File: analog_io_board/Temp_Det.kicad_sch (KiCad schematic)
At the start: 3 parts, among them J3 DG141R-02, U8 MAX31855KASA (SOIC-8)

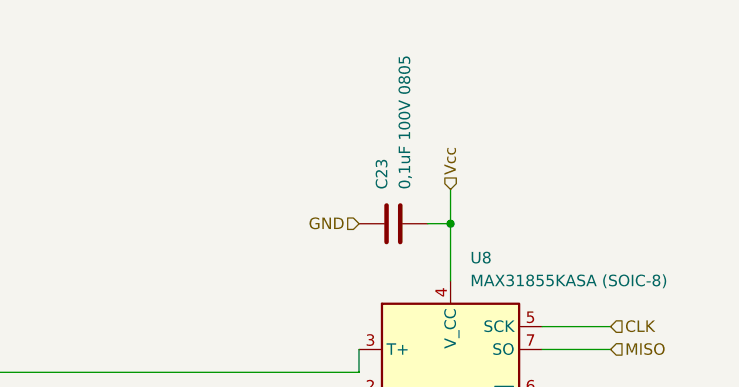
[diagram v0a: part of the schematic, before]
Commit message: all замменил резисторы failsafe в плате контроллера и обрал из перечня во всех остальных
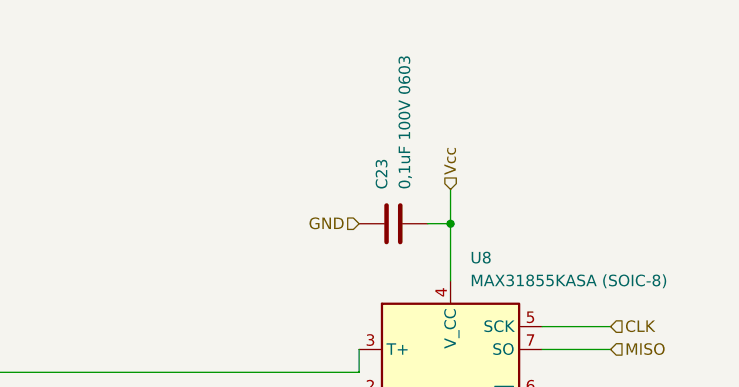
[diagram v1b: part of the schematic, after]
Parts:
- C23: value 0,1uF 100V 0805 -> 0,1uF 100V 0603; footprint Capacitor_SMD:C_0805_2012Metric_Pad1.18x1.45mm_HandSolder -> Capacitor_SMD:C_0603_1608Metric_Pad1.08x0.95mm_HandSolder

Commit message: analog board refresh
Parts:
- removed C23: 0,1uF 100V 0603, Capacitor_SMD:C_0603_1608Metric_Pad1.08x0.95mm_HandSolder, symbol Device:C
- removed J3: DG141R-02, Connector:DG141R-02, symbol Connector_Generic:Conn_01x02
- removed U8: MAX31855KASA (SOIC-8), Package_SO:SOIC-8_3.9x4.9mm_P1.27mm, symbol Sensor_Temperature:MAX31855KASA
- added C26, C27: 0,1uF 100V 0603, Capacitor_SMD:C_0603_1608Metric_Pad1.08x0.95mm_HandSolder, symbol Device:C
- added J5, J6: DG141R-2.54-03P-14-00A(H), symbol Connector:Conn_01x03_Socket
- added R18, R19, R20, R21: 0805-4,7 кОм±5%-0,125 Вт, PCM_4ms_Resistor:R_0805_2012Metric, symbol Device:R
- added TP21, TP22: TestPoint, PCM_4ms_TestPoint:TestPoint_D1, symbol Connector:TestPoint
- added U6, U8: DS18S20, Package_TO_SOT_THT:TO-92_Inline, symbol Sensor_Temperature:DS18S20
- added U7: π142M3x, Package_SO:SOIC-16_3.9x9.9mm_P1.27mm, symbol Isolator:π142M3x
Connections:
- new net: J6.2 (Pin_2), R19.1, TP22.1, U7.4 (VIB), U7.6 (VOD)
- new net: J5.2 (Pin_2), R18.1, TP21.1, U7.3 (VIA), U7.5 (VOC)
- new net: R20.2, U7.10 (VE2)
- new net: R21.1, U7.7 (VE1)
- new net +3.3VA: C27.2, J5.3 (Pin_3), J6.3 (Pin_3), R18.2, R19.2, R21.2, U7.1 (VDD1)
- new net +3V3: C26.2, R20.1, U7.16 (VDD2)
- new net GNDA: C27.1, J5.1 (Pin_1), J6.1 (Pin_1), U7.2 (GND1), U7.8 (GND1)
- new net GNDD: C26.1, U7.15 (GND2), U7.9 (GND2)
- new net RX_USART_2: U7.14 (VOA)
- new net RX_USART_4: U7.13 (VOB)
- new net TX_USART_2: U7.12 (VIC)
- new net TX_USART_4: U7.11 (VID)

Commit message: analog board refresh pcb
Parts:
- C26, C27: footprint Capacitor_SMD:C_0603_1608Metric_Pad1.08x0.95mm_HandSolder -> Capacitor_SMD:C_0603_1608Metric
- J6: footprint (none) -> Connector:DG141R-2.54-03P
- J7: renamed from J5; footprint (none) -> Connector:DG141R-2.54-03P
- R18, R19, R20, R21: footprint PCM_4ms_Resistor:R_0805_2012Metric -> Resistor_SMD:R_0805_2012Metric
- TP21, TP22: footprint PCM_4ms_TestPoint:TestPoint_D1 -> TestPoint:TestPoint_Pad_D1.0mm
- U7: value π142M3x -> PAI142M3x
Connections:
- no-connect marks 0 -> 6
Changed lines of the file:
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@@
 		(color 0 0 0 0)
+	)
+	(no_connect
+		(at 260.35 101.6)
+	)
+	(no_connect
+		(at 267.97 93.98)
+	)
+	(no_connect
+		(at 267.97 109.22)
+	)
+	(no_connect
+		(at 260.35 76.2)
+	)
+	(no_connect
+		(at 267.97 68.58)
+	)
+	(no_connect
+		(at 267.97 83.82)
 	)
 	(wire
@@
 			)
 		)
-		(property "Footprint" "PCM_4ms_TestPoint:TestPoint_D1"
+		(property "Footprint" "TestPoint:TestPoint_Pad_D1.0mm"
 			(at 137.16 83.82 0)
 			(effects
@@
 			)
 		)
-		(property "Description" ""
+		(property "Description" "test point"
 			(at 142.24 83.82 0)
 			(effects
@@
 			)
 		)
-		(property "Footprint" "PCM_4ms_Resistor:R_0805_2012Metric"
+		(property "Footprint" "Resistor_SMD:R_0805_2012Metric"
 			(at 166.878 99.06 90)
 			(effects
@@
 			)
 		)
-		(property "Description" ""
+		(property "Description" "Resistor"
 			(at 165.1 99.06 0)
 			(effects
@@
 			)
 		)
-		(property "Footprint" "PCM_4ms_Resistor:R_0805_2012Metric"
+		(property "Footprint" "Resistor_SMD:R_0805_2012Metric"
 			(at 163.322 73.66 90)
 			(effects
@@
 			)
 		)
-		(property "Description" ""
+		(property "Description" "Resistor"
 			(at 165.1 73.66 0)
 			(effects
@@
 			)
 		)
-		(property "Description" ""
+		(property "Description" "Power symbol creates a global label with name \"+3.3VA\""
 			(at 236.22 100.33 0)
 			(effects
@@
 	)
 	(symbol
-		(lib_id "PCM_4ms_Power-symbol:GNDA")
+		(lib_id "power:GNDA")
 		(at 114.3 73.66 0)
 		(mirror x)
@@
 			)
 		)
-		(property "Description" ""
+		(property "Description" "Power symbol creates a global label with name \"GNDA\" , analog ground"
 			(at 114.3 73.66 0)
 			(effects
@@
 			)
 		)
-		(property "Description" ""
+		(property "Description" "Power symbol creates a global label with name \"+3.3VA\""
 			(at 236.22 74.93 0)
 			(effects
@@
 		)
 		(property "Value" "GNDD"
-			(at 80.01 69.85 0)
+			(at 80.01 68.58 0)
 			(effects
 				(font
@@
 			)
 		)
-		(property "Description" ""
+		(property "Description" "Power symbol creates a global label with name \"GNDD\" , digital ground"
 			(at 80.01 73.66 0)
 			(effects
@@
 	)
 	(symbol
-		(lib_id "PCM_4ms_Power-symbol:GNDA")
+		(lib_id "power:GNDA")
 		(at 113.03 109.22 0)
 		(mirror y)
@@
 			)
 		)
-		(property "Description" ""
+		(property "Description" "Power symbol creates a global label with name \"GNDA\" , analog ground"
 			(at 113.03 109.22 0)
 			(effects
@@
 			)
 		)
-		(property "Description" ""
+		(property "Description" "Power symbol creates a global label with name \"GNDD\" , digital ground"
 			(at 45.72 132.08 0)
 			(effects
@@
 			)
 		)
-		(property "Value" "π142M3x"
+		(property "Value" "PAI142M3x"
 			(at 97.79 78.74 0)
 			(effects
@@
 			)
 		)
-		(property "Description" ""
+		(property "Description" "Power symbol creates a global label with name \"+3V3\""
 			(at 73.66 83.82 0)
 			(effects
@@
 			)
 		)
-		(property "Footprint" "Capacitor_SMD:C_0603_1608Metric_Pad1.08x0.95mm_HandSolder"
+		(property "Footprint" "Capacitor_SMD:C_0603_1608Metric"
 			(at 79.0448 81.28 0)
 			(effects
@@
 			)
 		)
-		(property "Description" ""
+		(property "Description" "Unpolarized capacitor"
 			(at 80.01 77.47 0)
 			(effects
@@
 			)
 		)
-		(property "Description" ""
+		(property "Description" "Power symbol creates a global label with name \"+3.3VA\""
 			(at 48.26 143.51 0)
 			(effects
@@
 			)
 		)
-		(property "Footprint" "PCM_4ms_Resistor:R_0805_2012Metric"
+		(property "Footprint" "Resistor_SMD:R_0805_2012Metric"
 			(at 118.11 99.822 90)
 			(effects
@@
 			)
 		)
-		(property "Description" ""
+		(property "Description" "Resistor"
 			(at 118.11 101.6 0)
 			(effects
@@
 		(dnp no)
 		(fields_autoplaced yes)
-		(property "Reference" "J5"
+		(property "Reference" "J7"
 			(at 240.665 69.85 0)
 			(effects
@@
 			)
 		)
-		(property "Footprint" ""
+		(property "Footprint" "Connector:DG141R-2.54-03P"
 			(at 241.3 77.47 0)
 			(effects
@@
 			(project "analog_io_board"
 				(path "/c658a069-2acb-41ac-8530-c56b14d342d1/c4e2dc63-ff36-4a03-a5b1-351b3374beb1"
-					(reference "J5")
+					(reference "J7")
 					(unit 1)
 				)
@@
 			)
 		)
-		(property "Description" ""
+		(property "Description" "Power symbol creates a global label with name \"GNDD\" , digital ground"
 			(at 82.55 107.95 0)
 			(effects
@@
 			)
 		)
-		(property "Description" ""
+		(property "Description" "Power symbol creates a global label with name \"+3V3\""
 			(at 45.72 124.46 0)
 			(effects
@@
 			)
 		)
-		(property "Description" ""
+		(property "Description" "Power symbol creates a global label with name \"+3.3VA\""
 			(at 115.57 83.82 0)
 			(effects
@@
 			)
 		)
-		(property "Footprint" ""
+		(property "Footprint" "Connector:DG141R-2.54-03P"
 			(at 241.3 102.87 0)
 			(effects
@@
 	)
 	(symbol
-		(lib_id "PCM_4ms_Power-symbol:GNDA")
+		(lib_id "power:GNDA")
 		(at 45.72 152.4 0)
 		(mirror y)
@@
 			)
 		)
-		(property "Description" ""
+		(property "Description" "Power symbol creates a global label with name \"GNDA\" , analog ground"
 			(at 45.72 152.4 0)
 			(effects
@@
 			)
 		)
-		(property "Description" ""
+		(property "Description" "Power symbol creates a global label with name \"+3V3\""
 			(at 72.39 101.6 0)
 			(effects
@@
 			)
 		)
-		(property "Footprint" "PCM_4ms_TestPoint:TestPoint_D1"
+		(property "Footprint" "TestPoint:TestPoint_Pad_D1.0mm"
 			(at 125.73 83.82 0)
 			(effects
@@
 			)
 		)
-		(property "Description" ""
+		(property "Description" "test point"
 			(at 130.81 83.82 0)
 			(effects
@@
 	)
 	(symbol
-		(lib_id "PCM_4ms_Power-symbol:GNDA")
+		(lib_id "power:GNDA")
 		(at 236.22 105.41 270)
 		(unit 1)
@@
 		)
 		(property "Value" "GNDA"
-			(at 232.41 105.4101 90)
+			(at 232.41 105.4099 90)
 			(effects
 				(font
@@
 			)
 		)
-		(property "Description" ""
+		(property "Description" "Power symbol creates a global label with name \"GNDA\" , analog ground"
 			(at 236.22 105.41 0)
 			(effects
@@
 			)
 		)
-		(property "Description" ""
+		(property "Description" "Power symbol creates a global label with name \"+3.3VA\""
 			(at 123.19 101.6 0)
 			(effects
@@
 	)
 	(symbol
-		(lib_id "PCM_4ms_Power-symbol:GNDA")
+		(lib_id "power:GNDA")
 		(at 236.22 80.01 270)
 		(unit 1)
@@
 		)
 		(property "Value" "GNDA"
-			(at 232.41 80.0101 90)
+			(at 232.41 80.0099 90)
 			(effects
 				(font
@@
 			)
 		)
-		(property "Description" ""
+		(property "Description" "Power symbol creates a global label with name \"GNDA\" , analog ground"
 			(at 236.22 80.01 0)
 			(effects
@@
 			)
 		)
-		(property "Description" ""
+		(property "Description" "Power symbol creates a global label with name \"+3.3VA\""
 			(at 165.1 104.14 0)
 			(effects
@@
 			)
 		)
-		(property "Footprint" "Capacitor_SMD:C_0603_1608Metric_Pad1.08x0.95mm_HandSolder"
+		(property "Footprint" "Capacitor_SMD:C_0603_1608Metric"
 			(at 113.3348 81.28 0)
 			(effects
@@
 			)
 		)
-		(property "Description" ""
+		(property "Description" "Unpolarized capacitor"
 			(at 114.3 77.47 0)
 			(effects
@@
 			)
 		)
-		(property "Description" ""
+		(property "Description" "Power symbol creates a global label with name \"+3.3VA\""
 			(at 165.1 68.58 0)
 			(effects
@@
 			)
 		)
-		(property "Footprint" "PCM_4ms_Resistor:R_0805_2012Metric"
+		(property "Footprint" "Resistor_SMD:R_0805_2012Metric"
 			(at 76.2 99.822 90)
 			(effects
@@
 			)
 		)
-		(property "Description" ""
+		(property "Description" "Resistor"
 			(at 76.2 101.6 0)
 			(effects
